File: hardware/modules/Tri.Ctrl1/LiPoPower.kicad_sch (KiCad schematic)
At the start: 26 parts, among them SW901 Power Switch, U901 INA226, U902 TPS63070RNMR, U903 INA226

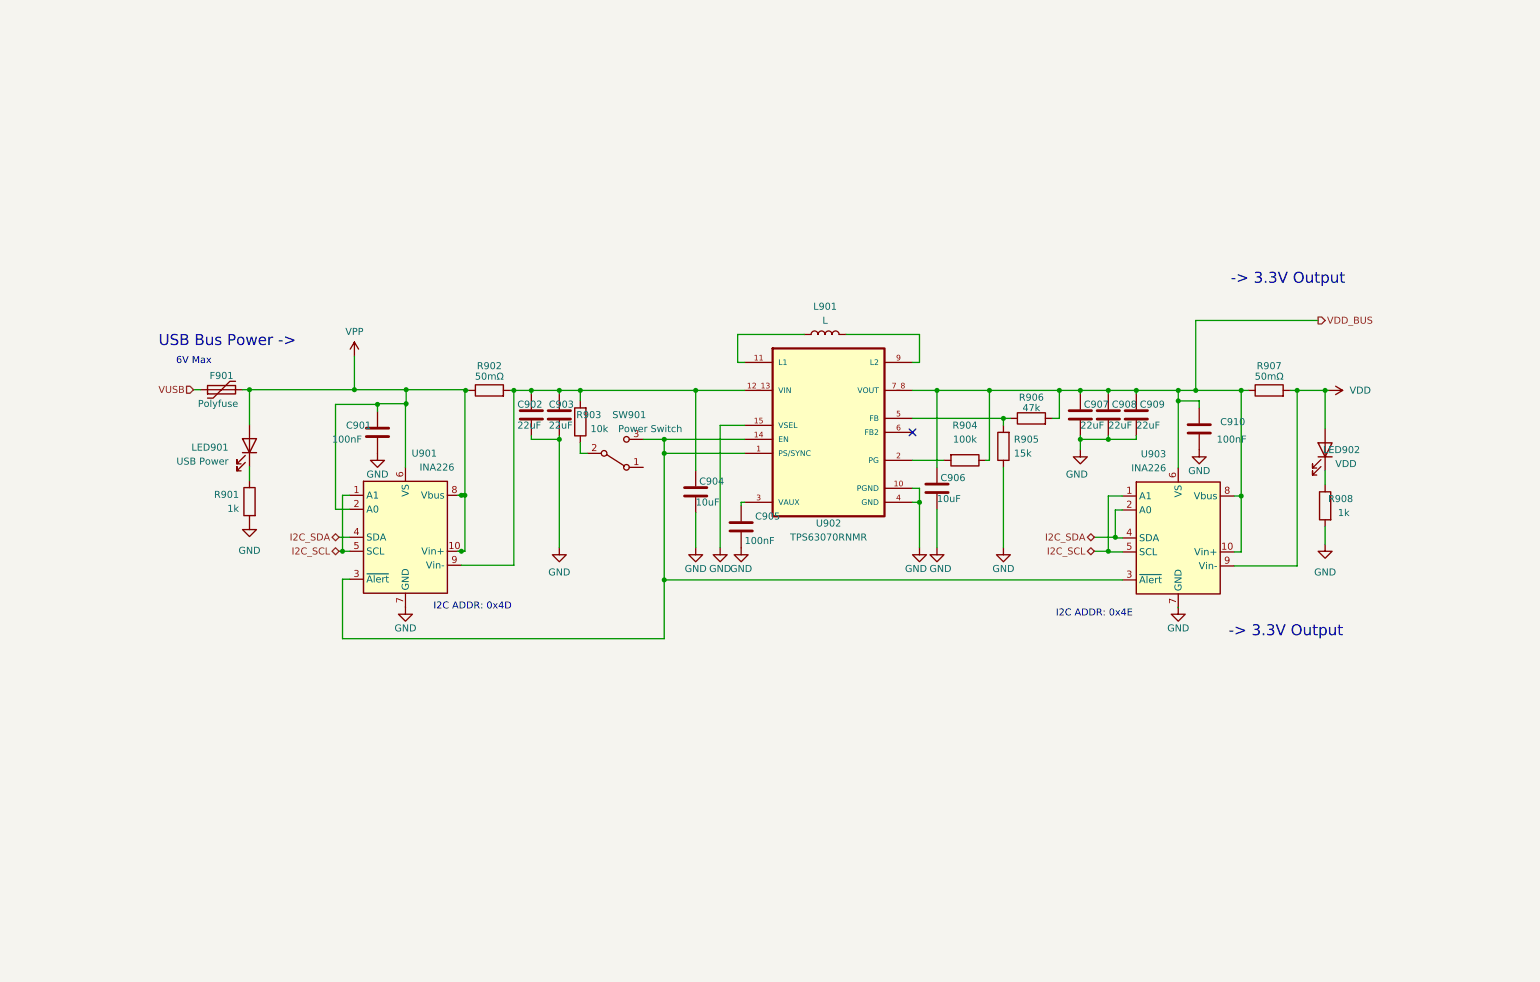
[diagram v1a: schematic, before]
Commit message: 電源回路をlipoの充放電込みのモノに変更
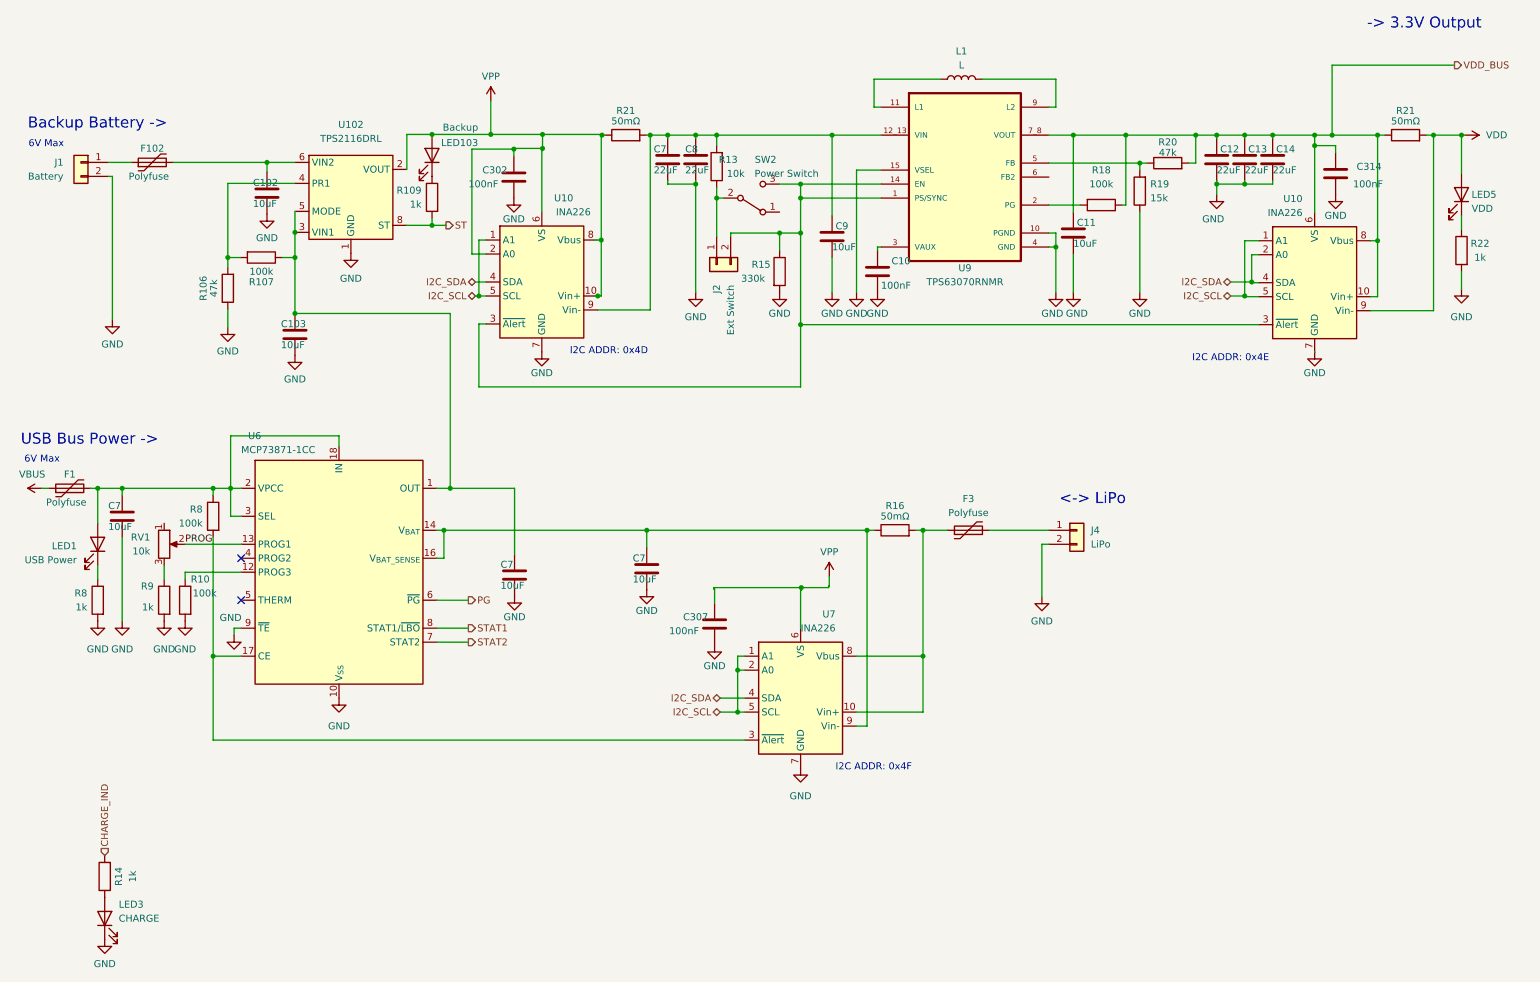
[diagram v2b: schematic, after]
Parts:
- removed C901, C905, C910: 100nF, Capacitor_SMD:C_0402_1005Metric, symbol Device:C
- removed C902, C903, C907, C908, C909: 22uF, Capacitor_SMD:C_0805_2012Metric, symbol Device:C
- removed C904, C906: 10uF, Capacitor_SMD:C_0603_1608Metric, symbol Device:C
- removed F901: Polyfuse, Fuse:Fuse_1206_3216Metric, symbol Device:Polyfuse
- removed L901: L, Inductor_SMD:L_Wuerth_WE-TPC-3816, symbol Device:L
- removed LED901: USB Power, LED_SMD:LED_0805_2012Metric, symbol Device:LED
- removed LED902: VDD, LED_SMD:LED_0805_2012Metric, symbol Device:LED
- removed R901, R908: 1k, Resistor_SMD:R_0402_1005Metric, symbol Device:R
- removed R902, R907: 50mΩ, Resistor_SMD:R_0805_2012Metric, symbol Device:R
- removed R903: 10k, Resistor_SMD:R_0402_1005Metric, symbol Device:R
- removed R904: 100k, Resistor_SMD:R_0402_1005Metric, symbol Device:R
- removed R905: 15k, Resistor_SMD:R_0402_1005Metric, symbol Device:R
- removed R906: 47k, Resistor_SMD:R_0402_1005Metric, symbol Device:R
- removed SW901: Power Switch, Button_Switch_THT:SW_Slide_SPDT_Angled_CK_OS102011MA1Q, symbol Switch:SW_SPDT
- removed U901, U903: INA226, Package_SO:VSSOP-10_3x3mm_P0.5mm, symbol Sensor_Energy:INA226
- removed U902: TPS63070RNMR, WOBCLibrary:VREG_TPS63070RNMR, symbol WOBCLibrary:TPS63070RNMR
- added C10, C302, C307, C314: 100nF, Capacitor_SMD:C_0402_1005Metric, symbol Device:C
- added C102, C103, C11, C7 (x3), C9: 10uF, Capacitor_SMD:C_0603_1608Metric, symbol Device:C
- added C12, C13, C14, C7, C8: 22uF, Capacitor_SMD:C_0805_2012Metric, symbol Device:C
- added F1, F102, F3: Polyfuse, Fuse:Fuse_1206_3216Metric, symbol Device:Polyfuse
- added J1: Battery, Connector_JST:JST_XH_S2B-XH-A_1x02_P2.50mm_Horizontal, symbol Connector_Generic:Conn_01x02
- added J2: Ext Switch, Connector_JST:JST_PH_S2B-PH-K_1x02_P2.00mm_Horizontal, symbol Connector_Generic:Conn_01x02
- added J4: LiPo, Connector_JST:JST_PH_S2B-PH-K_1x02_P2.00mm_Horizontal, symbol Connector_Generic:Conn_01x02
- added L1: L, Inductor_SMD:L_Wuerth_WE-TPC-3816, symbol Device:L
- added LED1: USB Power, LED_SMD:LED_0805_2012Metric, symbol Device:LED
- added LED103: Backup, LED_SMD:LED_0805_2012Metric, symbol Device:LED
- added LED3: CHARGE, LED_SMD:LED_0805_2012Metric, symbol Device:LED
- added LED5: VDD, LED_SMD:LED_0805_2012Metric, symbol Device:LED
- added R10, R107, R18, R8: 100k, Resistor_SMD:R_0402_1005Metric, symbol Device:R
- added R106, R20: 47k, Resistor_SMD:R_0402_1005Metric, symbol Device:R
- added R109, R14, R22, R8, R9: 1k, Resistor_SMD:R_0402_1005Metric, symbol Device:R
- added R13: 10k, Resistor_SMD:R_0402_1005Metric, symbol Device:R
- added R15: 330k, Resistor_SMD:R_0402_1005Metric, symbol Device:R
- added R16, R21 (x2): 50mΩ, Resistor_SMD:R_0805_2012Metric, symbol Device:R
- added R19: 15k, Resistor_SMD:R_0402_1005Metric, symbol Device:R
- added RV1: 10k, Potentiometer_SMD:Potentiometer_Bourns_TC33X_Vertical, symbol Device:R_Potentiometer
- added SW2: Power Switch, Button_Switch_THT:SW_CuK_OS102011MA1QN1_SPDT_Angled, symbol Switch:SW_SPDT
- added U10 (x2), U7: INA226, Package_SO:VSSOP-10_3x3mm_P0.5mm, symbol Sensor_Energy:INA226
- added U102: TPS2116DRL, Package_TO_SOT_SMD:SOT-583-8, symbol Power_Management:TPS2116DRL
- added U6: MCP73871-1CC, Package_DFN_QFN:QFN-20-1EP_4x4mm_P0.5mm_EP2.5x2.5mm, symbol Battery_Management:MCP73871-1CC
- added U9: TPS63070RNMR, WOBCLibrary:VREG_TPS63070RNMR, symbol WOBCLibrary:TPS63070RNMR
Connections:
- net GND: now also C10.2, C102.2, C103.2, C11.2, C12.2, C13.2, C14.2, C302.2, C307.2, C314.2, C7.2, C7.2, C7.2, C7.2, C8.2, C9.2, J1.2 (Pin_2), J4.2 (Pin_2), LED3.1 (K), R10.2, R106.1, R15.2, R19.1, R22.2, R8.2, R9.2, U10.7 (GND), U10.7 (GND), U102.1 (GND), U6.10 (V_{SS}), U6.11 (V_{SS}), U6.21 (V_{SS}), U6.9 (~{TE}), U7.7 (GND), U9.10 (PGND), U9.15 (VSEL), U9.4 (GND)
- net I2C_SCL: now also U10.1 (A1), U10.1 (A1), U10.5 (SCL), U10.5 (SCL), U7.1 (A1), U7.2 (A0), U7.5 (SCL)
- net I2C_SDA: now also U10.2 (A0), U10.4 (SDA), U10.4 (SDA), U7.4 (SDA)
- net VDD: now also LED5.2 (A), R21.2, U10.9 (Vin-)
- net VDD_BUS: now also C11.1, C12.1, C13.1, C14.1, C314.1, R18.1, R20.2, R21.1, U10.10 (Vin+), U10.6 (VS), U10.8 (Vbus), U9.7_8 (VOUT)
- net VPP: now also C302.1, C307.1, LED103.2 (A), R21.1, U10.10 (Vin+), U10.2 (A0), U10.6 (VS), U102.2 (VOUT), U102.7 (VOUT), U7.6 (VS)
- new net: C102.1, F102.2, U102.6 (VIN2)
- new net: C7.1, F1.2, LED1.2 (A), R8.1, U6.18 (IN), U6.19 (IN), U6.2 (VPCC), U6.3 (SEL)
- new net: LED5.1 (K), R22.1
- new net: C7.1, C8.1, C9.1, R13.2, R21.2, U10.9 (Vin-), U9.12_13 (VIN)
- new net: J2.2 (Pin_2), R15.1, SW2.3 (C), U10.3 (~{Alert}), U10.3 (~{Alert}), U9.1 (PS/SYNC), U9.14 (EN)
- new net: LED1.1 (K), R8.1
- new net: L1.1, U9.11 (L1)
- new net: L1.2, U9.9 (L2)
- new net: F3.2, J4.1 (Pin_1)
- new net: C103.1, C7.1, R107.1, U102.3 (VIN1), U102.5 (MODE), U6.1 (OUT), U6.20 (OUT)
- new net: R106.2, R107.2, U102.4 (PR1)
- new net: R19.2, R20.1, U9.5 (FB)
- new net: C10.1, U9.3 (VAUX)
- new net: C7.1, R16.1, U6.14 (V_{BAT}), U6.15 (V_{BAT}), U6.16 (V_{BAT_SENSE}), U7.9 (Vin-)
- new net: F3.1, R16.2, U7.10 (Vin+), U7.8 (Vbus)
- new net: R9.1, RV1.3
- new net: LED3.2 (A), R14.1
- new net: F102.1, J1.1 (Pin_1)
- new net: R18.2, U9.2 (PG)
- new net: J2.1 (Pin_1), R13.1, SW2.2 (B)
- new net: R8.2, U6.17 (CE), U7.3 (~{Alert})
- new net: LED103.1 (K), R109.1
- new net: R10.1, U6.12 (PROG3)
- new net CHARGE_IND: R14.2
- new net PG: U6.6 (~{PG})
- new net PROG: RV1.2, U6.13 (PROG1)
- new net ST: R109.2, U102.8 (ST)
- new net STAT1: U6.8 (STAT1/~{LBO})
- new net STAT2: U6.7 (STAT2)
- new net VBUS: F1.1
- no-connect marks 1 -> 2
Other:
- note added: "<-> LiPo"
- note added: "Backup Battery ->"
- note added: "I2C ADDR: 0x4F"

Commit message: バックアップの回路削除
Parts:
- removed C102, C103: 10uF, Capacitor_SMD:C_0603_1608Metric, symbol Device:C
- removed F102: Polyfuse, Fuse:Fuse_1206_3216Metric, symbol Device:Polyfuse
- removed J1: Battery, Connector_JST:JST_XH_S2B-XH-A_1x02_P2.50mm_Horizontal, symbol Connector_Generic:Conn_01x02
- removed J2: Ext Switch, Connector_JST:JST_PH_S2B-PH-K_1x02_P2.00mm_Horizontal, symbol Connector_Generic:Conn_01x02
- removed LED103: Backup, LED_SMD:LED_0805_2012Metric, symbol Device:LED
- removed R106: 47k, Resistor_SMD:R_0402_1005Metric, symbol Device:R
- removed R107: 100k, Resistor_SMD:R_0402_1005Metric, symbol Device:R
- removed R109: 1k, Resistor_SMD:R_0402_1005Metric, symbol Device:R
- removed U102: TPS2116DRL, Package_TO_SOT_SMD:SOT-583-8, symbol Power_Management:TPS2116DRL
- J501: renamed from J4; footprint Connector_JST:JST_PH_S2B-PH-K_1x02_P2.00mm_Horizontal -> Connector_JST:JST_XA_B02B-XASK-1_1x02_P2.50mm_Vertical
- SW501: renamed from SW2; footprint Button_Switch_THT:SW_CuK_OS102011MA1QN1_SPDT_Angled -> Button_Switch_THT:SW_Slide_SPDT_Straight_CK_OS102011MS2Q
- renumbered C7 to C501, C302 to C502, C7 to C503, C7 to C504, C7 to C505, C8 to C506, C307 to C507, C9 to C508, C10 to C509, C11 to C510, C12 to C511, C13 to C512, C14 to C513, C314 to C514, F1 to F501, F3 to F502, L1 to L501, LED1 to LED501, LED3 to LED502, LED5 to LED503, R8 to R501, R14 to R502, R9 to R503, R10 to R504, R8 to R505, R21 to R506, R13 to R507, R15 to R508, R16 to R509, R18 to R510, R19 to R511, R20 to R512, R21 to R513, R22 to R514, RV1 to RV501, U6 to U501, U10 to U502, U7 to U503, U9 to U504, U10 to U505
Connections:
- net VPP: now also C503.1, U501.1 (OUT), U501.20 (OUT)
- no-connect marks 2 -> 3
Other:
- note removed: "Backup Battery ->"

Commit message: 一通り配置
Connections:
- net VDD: now also C502.1, C507.1, U502.2 (A0), U502.6 (VS), U503.6 (VS)
- net VPP: now also U502.8 (Vbus); no longer C502.1, C507.1, U502.2 (A0), U502.6 (VS), U503.6 (VS)
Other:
- moved on the sheet: C507

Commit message: 主にCAN周りの修正
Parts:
- added R505: 10k, Resistor_SMD:R_0402_1005Metric, symbol Device:R
- renumbered R505 to R506, R506 to R507, R507 to R508, R508 to R509, R509 to R510, R510 to R511, R511 to R512, R512 to R513, R513 to R514, R514 to R515
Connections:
- net GND: now also R505.2
- net at U501.5 (THERM): now also R505.1
- no-connect marks 3 -> 2

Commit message: LCSC一部修正
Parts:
- F501, F502: LCSC C883133 -> C883133
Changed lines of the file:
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@@
 			)
 		)
-		(property "LCSC" " C883133"
+		(property "LCSC" "C883133"
 			(at 22.86 101.6 0)
 			(effects
@@
 			)
 		)
-		(property "LCSC" " C883133"
+		(property "LCSC" "C883133"
 			(at 186.055 109.22 0)
 			(effects

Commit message: LCSC最終確認
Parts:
- R509: LCSC C23137 -> C25778
- U501: LCSC C511310 -> C511310
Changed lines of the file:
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@@
 			)
 		)
-		(property "LCSC" "C23137"
+		(property "LCSC" "C25778"
 			(at 151.765 62.23 0)
 			(effects
@@
 			)
 		)
-		(property "LCSC" " C511310"
+		(property "LCSC" "C511310"
 			(at 71.755 116.84 0)
 			(effects

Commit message: ガーバー作り直し
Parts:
- U504: value TPS63070RNMR -> TPS63070RNMT; LCSC C109322 -> C964639
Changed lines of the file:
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@@
 	(wire
 		(pts
-			(xy 80.01 37.592) (xy 97.155 37.592)
+			(xy 80.01 37.465) (xy 97.155 37.465)
 		)
 		(stroke
@@
 	(wire
 		(pts
-			(xy 97.155 37.592) (xy 97.155 37.338)
+			(xy 97.155 37.465) (xy 97.155 37.338)
 		)
 		(stroke
@@
 	(wire
 		(pts
-			(xy 80.01 37.592) (xy 80.01 71.12)
+			(xy 80.01 37.465) (xy 80.01 71.12)
 		)
 		(stroke
@@
 			)
 		)
-		(property "Value" "TPS63070RNMR"
+		(property "Value" "TPS63070RNMT"
 			(at 185.42 64.135 0)
 			(effects
@@
 			)
 		)
-		(property "LCSC" "C109322"
+		(property "LCSC" "C964639"
 			(at 185.42 45.085 0)
 			(effects
